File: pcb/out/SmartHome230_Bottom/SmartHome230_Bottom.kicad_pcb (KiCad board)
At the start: 2 copper layers, 130 x 115 mm, 58 parts, among them J1 B2B, J2 12V, J3 Przyciski A, J4 Przyciski B, J5 UART, J6 230V IN, J7 Wyj.1, J8 Wyj.2, K1 SRD-12V, K2 SRD-12V, Q1 BC547, Q2 BC547, SW1 EN, SW2 BOOT, U1 MP1584, U2 AMS1117-3.3, U3 ESP32-WROOM-32

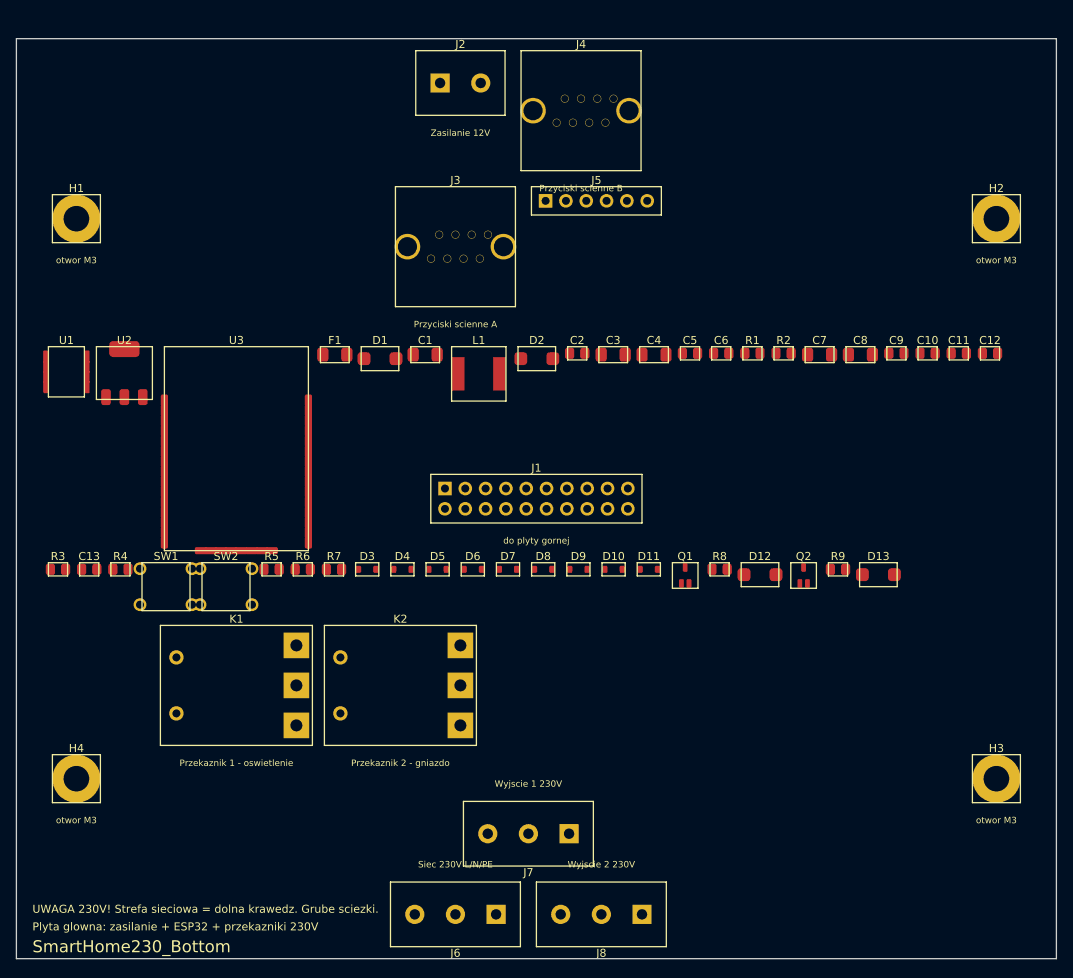
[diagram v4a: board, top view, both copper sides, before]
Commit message: Wiecej RJ45 (8 podwojnych=64 wej), zabezpieczenia, zlacza na obu krawedziach
- Wejscia: 8 podwojnych RJ45 = 16 portow = 64 wejscia (4 ekspandery MCP23017).
- Zabezpieczenia: PTC na kazde z 16 wyjsc, MOV na wyjsciach 230V, snubber RC na
  stykach przekaznikow, dlawik wspolny (CMC) + TVS na RS485/CAN, TVS na wyjsciach DC.
  Nowe czesci: PTC (polyfuse), CMC (common-mode choke).
- Layout: zlacza rozlozone na GORNA i DOLNA krawedz (_split_balanced) -> wezsza
  plytka; gestsze upakowanie, mniejszy luz wysokosci. auto_frame liczy szerokosc
  z rozlozenia na 2 krawedzie. HomeCtrlPro: 237 -> 155 mm szerokosci.

Oba PCB 0/0/0, testy 12/12, kiutils OK.

Co-Authored-By: Claude Opus 4.8 (1M context) <noreply@anthropic.com>
Claude-Session: https://claude.ai/code/session_01LNGxtK2Jv1rJLBLPTwFQ9C
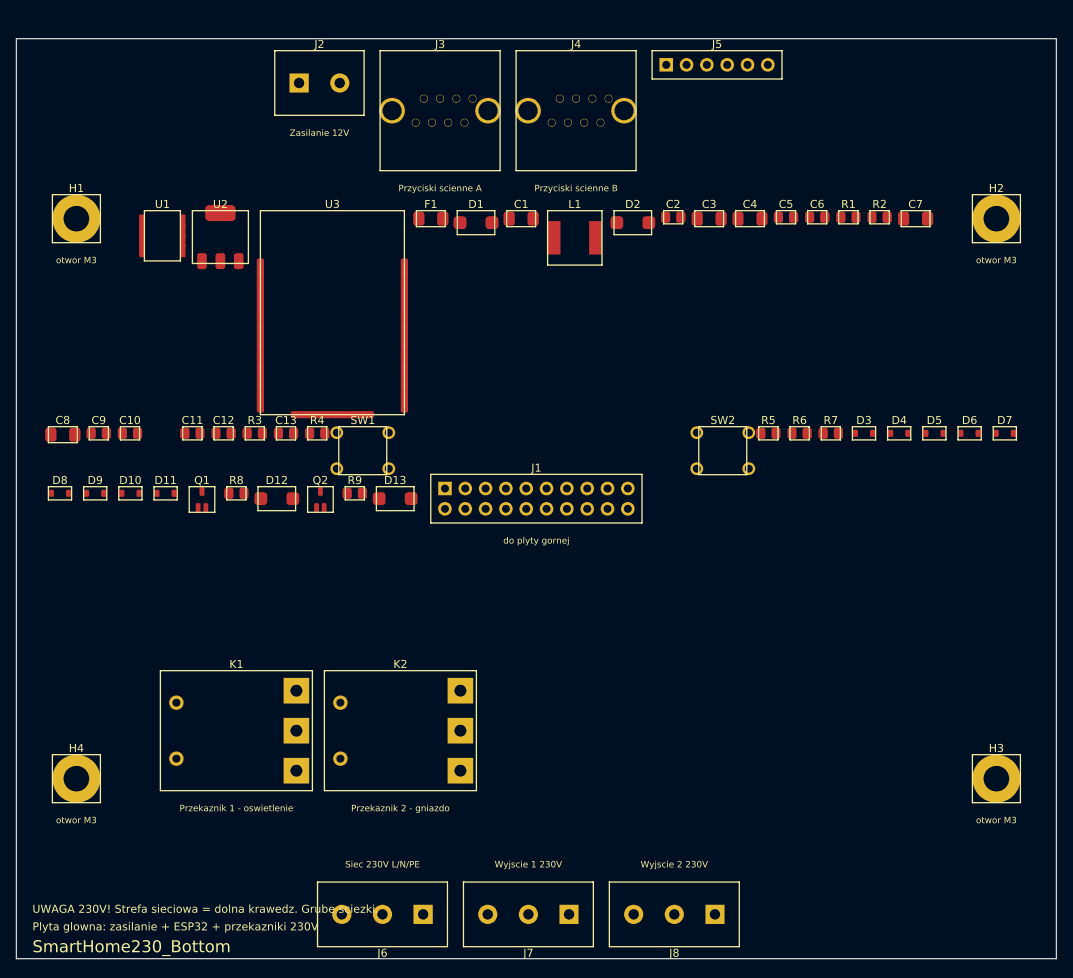
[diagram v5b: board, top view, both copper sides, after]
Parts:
- moved C10 100.2 mm to (14.2, 49.3)
- moved C8 100.2 mm to (5.80, 49.5)
- moved C9 100.2 mm to (10.3, 49.3)
- moved C12 96.3 mm to (25.9, 49.3)
- moved C11 96.3 mm to (22.0, 49.3)
- moved D3 64.4 mm to (106.0, 49.3)
- moved D5 64.4 mm to (114.8, 49.3)
- moved R5 64.4 mm to (94.0, 49.3)
- moved D4 64.4 mm to (110.3, 49.3)
- moved D6 64.4 mm to (119.2, 49.3)
- moved D7 64.4 mm to (123.5, 49.3)
- moved R6 64.4 mm to (97.9, 49.3)
- moved R7 64.4 mm to (101.8, 49.3)
- moved SW2 64.4 mm to (88.3, 51.5)
- moved D10 61.1 mm to (14.2, 56.8)
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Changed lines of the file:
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@@
     "pcbforge:ScrewTerminal_1x02_P5.08mm"
     (layer "F.Cu")
-    (at 55.5 5.54)
+    (at 37.88 5.54)
     (descr "Listwa zaciskowa 2x5.08mm")
     (attr through_hole)
@@
     "pcbforge:RJ45_8P8C"
     (layer "F.Cu")
-    (at 54.88 26)
+    (at 52.96 9)
     (descr "Gniazdo RJ45 8P8C THT")
     (attr through_hole)
@@
     "pcbforge:RJ45_8P8C"
     (layer "F.Cu")
-    (at 70.58 9)
+    (at 69.96 9)
     (descr "Gniazdo RJ45 8P8C THT")
     (attr through_hole)
@@
     "pcbforge:F_1206"
     (layer "F.Cu")
-    (at 39.8 39.5)
+    (at 51.8 22.5)
     (descr "F chip 1206")
     (attr smd)
@@
     "pcbforge:D_SMA"
     (layer "F.Cu")
-    (at 45.45 40)
+    (at 57.45 23)
     (descr "D_SMA")
     (attr smd)
@@
     "pcbforge:CP_1206"
     (layer "F.Cu")
-    (at 51.1 39.5)
+    (at 63.1 22.5)
     (descr "CP chip 1206")
     (attr smd)
@@
     "pcbforge:SOIC-8"
     (layer "F.Cu")
-    (at 6.25 41.64)
+    (at 18.25 24.64)
     (descr "SOIC-8 (1.27mm)")
     (attr smd)
@@
     "pcbforge:L_6x6"
     (layer "F.Cu")
-    (at 57.8 41.9)
+    (at 69.8 24.9)
     (descr "Cewka mocy 6x6mm")
     (attr smd)
@@
     "pcbforge:D_SMA"
     (layer "F.Cu")
-    (at 65.05 40)
+    (at 77.05 23)
     (descr "D_SMA")
     (attr smd)
@@
     "pcbforge:C_0805"
     (layer "F.Cu")
-    (at 70.1 39.33)
+    (at 82.1 22.32)
     (descr "C chip 0805")
     (attr smd)
@@
     "pcbforge:CP_1206"
     (layer "F.Cu")
-    (at 74.6 39.5)
+    (at 86.6 22.5)
     (descr "CP chip 1206")
     (attr smd)
@@
     "pcbforge:CP_1206"
     (layer "F.Cu")
-    (at 79.7 39.5)
+    (at 91.7 22.5)
     (descr "CP chip 1206")
     (attr smd)
@@
     "pcbforge:C_0805"
     (layer "F.Cu")
-    (at 84.2 39.33)
+    (at 96.2 22.32)
     (descr "C chip 0805")
     (attr smd)
@@
     "pcbforge:C_0805"
     (layer "F.Cu")
-    (at 88.1 39.33)
+    (at 100.1 22.32)
     (descr "C chip 0805")
     (attr smd)
@@
     "pcbforge:R_0805"
     (layer "F.Cu")
-    (at 92 39.33)
+    (at 104 22.32)
     (descr "R chip 0805")
     (attr smd)
@@
     "pcbforge:R_0805"
     (layer "F.Cu")
-    (at 95.9 39.33)
+    (at 107.9 22.32)
     (descr "R chip 0805")
     (attr smd)
@@
     "pcbforge:SOT-223"
     (layer "F.Cu")
-    (at 13.5 41.8)
+    (at 25.5 24.8)
     (descr "SOT-223 (regulator LDO)")
     (attr smd)
@@
     "pcbforge:CP_1206"
     (layer "F.Cu")
-    (at 100.4 39.5)
+    (at 112.4 22.5)
     (descr "CP chip 1206")
     (attr smd)
@@
     "pcbforge:CP_1206"
     (layer "F.Cu")
-    (at 105.5 39.5)
+    (at 5.8 49.5)
     (descr "CP chip 1206")
     (attr smd)
@@
     "pcbforge:C_0805"
     (layer "F.Cu")
-    (at 110 39.33)
+    (at 10.3 49.33)
     (descr "C chip 0805")
     (attr smd)
@@
     "pcbforge:C_0805"
     (layer "F.Cu")
-    (at 113.9 39.33)
+    (at 14.2 49.33)
     (descr "C chip 0805")
     (attr smd)
@@
     "pcbforge:ESP32-WROOM-32"
     (layer "F.Cu")
-    (at 27.5 51.25)
+    (at 39.5 34.25)
     (descr "Modul ESP32-WROOM-32 (38 padow)")
     (attr smd)
@@
     "pcbforge:C_0805"
     (layer "F.Cu")
-    (at 117.8 39.33)
+    (at 22 49.33)
     (descr "C chip 0805")
     (attr smd)
@@
     "pcbforge:C_0805"
     (layer "F.Cu")
-    (at 121.7 39.33)
+    (at 25.9 49.33)
     (descr "C chip 0805")
     (attr smd)
@@
     "pcbforge:R_0805"
     (layer "F.Cu")
-    (at 5.2 66.33)
+    (at 29.8 49.33)
     (descr "R chip 0805")
     (attr smd)
@@
     "pcbforge:C_0805"
     (layer "F.Cu")
-    (at 9.1 66.33)
+    (at 33.7 49.33)
     (descr "C chip 0805")
     (attr smd)
@@
     "pcbforge:R_0805"
     (layer "F.Cu")
-    (at 13 66.33)
+    (at 37.6 49.33)
     (descr "R chip 0805")
     (attr smd)
@@
     "pcbforge:SW_Push_6mm"
     (layer "F.Cu")
-    (at 18.7 68.5)
+    (at 43.3 51.5)
     (descr "Tact switch 6mm")
     (attr through_hole)
@@
     "pcbforge:SW_Push_6mm"
     (layer "F.Cu")
-    (at 26.2 68.5)
+    (at 88.3 51.5)
     (descr "Tact switch 6mm")
     (attr through_hole)
@@
     "pcbforge:PinHeader_1x06_P2.54mm"
     (layer "F.Cu")
-    (at 72.5 20.27)
+    (at 87.58 3.27)
     (descr "Pin header 1x6")
     (attr through_hole)
@@
     "pcbforge:R_0805"
     (layer "F.Cu")
-    (at 31.9 66.33)
+    (at 94 49.33)
     (descr "R chip 0805")
     (attr smd)
@@
     "pcbforge:R_0805"
     (layer "F.Cu")
-    (at 35.8 66.33)
+    (at 97.9 49.33)
     (descr "R chip 0805")
     (attr smd)
@@
     "pcbforge:R_0805"
     (layer "F.Cu")
-    (at 39.7 66.33)
+    (at 101.8 49.33)
     (descr "R chip 0805")
     (attr smd)
@@
     "pcbforge:D_SOD-323"
     (layer "F.Cu")
-    (at 43.85 66.33)
+    (at 105.95 49.33)
     (descr "D_SOD-323")
     (attr smd)
@@
     "pcbforge:D_SOD-323"
     (layer "F.Cu")
-    (at 48.25 66.33)
+    (at 110.35 49.33)
     (descr "D_SOD-323")
     (attr smd)
@@
     "pcbforge:D_SOD-323"
     (layer "F.Cu")
-    (at 52.65 66.33)
+    (at 114.75 49.33)
     (descr "D_SOD-323")
     (attr smd)
@@
     "pcbforge:D_SOD-323"
     (layer "F.Cu")
-    (at 57.05 66.33)
+    (at 119.15 49.33)
     (descr "D_SOD-323")
     (attr smd)
@@
     "pcbforge:D_SOD-323"
     (layer "F.Cu")
-    (at 61.45 66.33)
+    (at 123.55 49.33)
     (descr "D_SOD-323")
     (attr smd)
@@
     "pcbforge:D_SOD-323"
     (layer "F.Cu")
-    (at 65.85 66.33)
+    (at 5.45 56.83)
     (descr "D_SOD-323")
     (attr smd)
@@
     "pcbforge:D_SOD-323"
     (layer "F.Cu")
-    (at 70.25 66.33)
+    (at 9.85 56.83)
     (descr "D_SOD-323")
     (attr smd)
@@
     "pcbforge:D_SOD-323"
     (layer "F.Cu")
-    (at 74.65 66.33)
+    (at 14.25 56.83)
     (descr "D_SOD-323")
     (attr smd)
@@
     "pcbforge:D_SOD-323"
     (layer "F.Cu")
-    (at 79.05 66.33)
+    (at 18.65 56.83)
     (descr "D_SOD-323")
     (attr smd)
@@
     "pcbforge:ScrewTerminal_1x03_P5.08mm"
     (layer "F.Cu")
-    (at 54.88 109.46 180)
+    (at 45.76 109.46 180)
     (descr "Listwa zaciskowa 3x5.08mm")
     (attr through_hole)
@@
     "pcbforge:Relay_SPDT_SRD"
     (layer "F.Cu")
-    (at 27.5 80.84)
+    (at 27.5 86.5)
     (descr "Przekaznik SRD SPDT (cewka + kontakty 230V)")
     (attr through_hole)
@@
     "pcbforge:SOT-23-3"
     (layer "F.Cu")
-    (at 83.6 67.1)
+    (at 23.2 57.6)
     (descr "SOT-23-3")
     (attr smd)
@@
     "pcbforge:R_0805"
     (layer "F.Cu")
-    (at 87.9 66.33)
+    (at 27.5 56.83)
     (descr "R chip 0805")
     (attr smd)
@@
     "pcbforge:D_SMA"
     (layer "F.Cu")
-    (at 92.95 67)
+    (at 32.55 57.5)
     (descr "D_SMA")
     (attr smd)
@@
     "pcbforge:Relay_SPDT_SRD"
     (layer "F.Cu")
-    (at 48 80.84)
+    (at 48 86.5)
     (descr "Przekaznik SRD SPDT (cewka + kontakty 230V)")
     (attr through_hole)
@@
     "pcbforge:SOT-23-3"
     (layer "F.Cu")
-    (at 98.4 67.1)
+    (at 38 57.6)
     (descr "SOT-23-3")
     (attr smd)
@@
     "pcbforge:R_0805"
     (layer "F.Cu")
-    (at 102.7 66.33)
+    (at 42.3 56.83)
     (descr "R chip 0805")
     (attr smd)
@@
     "pcbforge:D_SMA"
     (layer "F.Cu")
-    (at 107.75 67)
+    (at 47.35 57.5)
     (descr "D_SMA")
     (attr smd)
@@
     "pcbforge:ScrewTerminal_1x03_P5.08mm"
     (layer "F.Cu")
-    (at 64 99.38 180)
+    (at 64 109.46 180)
     (descr "Listwa zaciskowa 3x5.08mm")
     (attr through_hole)
@@
     "pcbforge:ScrewTerminal_1x03_P5.08mm"
     (layer "F.Cu")
-    (at 73.12 109.46 180)
+    (at 82.24 109.46 180)
     (descr "Listwa zaciskowa 3x5.08mm")
     (attr through_hole)
